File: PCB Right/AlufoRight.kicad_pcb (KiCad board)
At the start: 2 copper layers, 139.7 x 90.9 mm, 67 parts, among them J10 Shield_Connection, J2 USB_C_Receptacle_USB2.0_16P_2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, J4 USB_C_Receptacle_USB2.0_16P_2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, J6 Shield_Connection, J8 Shield_Connection, K11 PG1350, K12 PG1350, K13 PG1350, K14 PG1350, K15 PG1350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

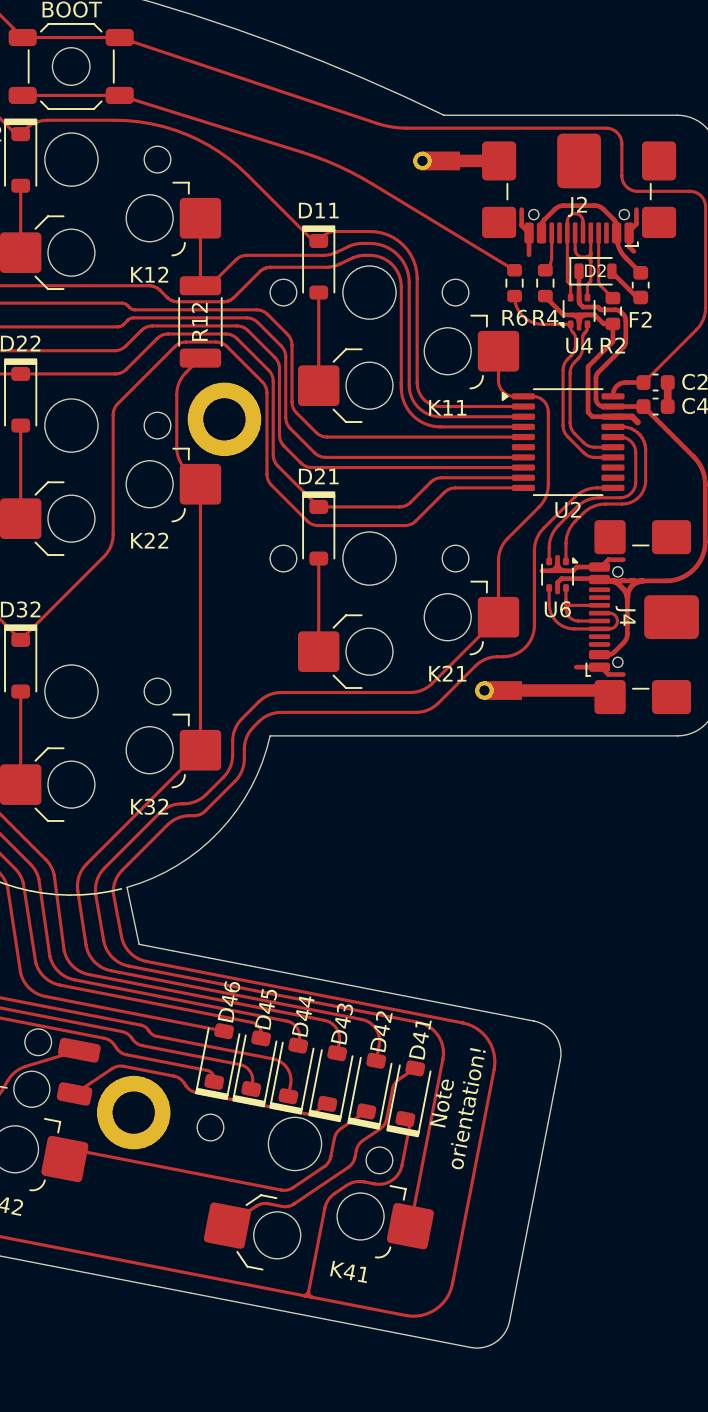
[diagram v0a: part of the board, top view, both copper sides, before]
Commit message: Tweak positioning of shield connections
Should now be the same on each side and align with other elements.
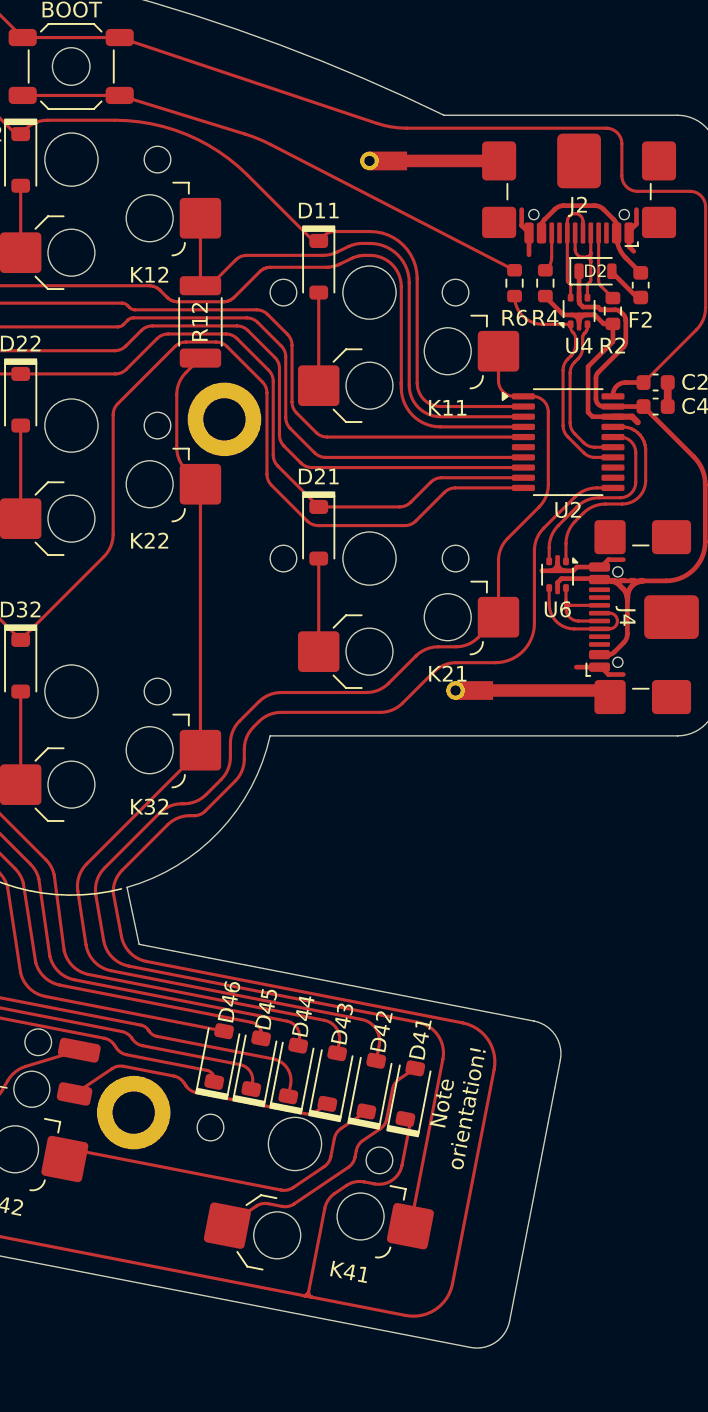
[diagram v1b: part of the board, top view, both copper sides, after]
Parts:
- moved J6 3.39 mm to (143.8, 44.0)
- moved J8 1.84 mm to (149.3, 77.9)
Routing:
- net Net-(J6-Pin_1): track 3.70 -> 7.09 mm
- net Net-(J8-Pin_1): track 6.41 -> 8.26 mm

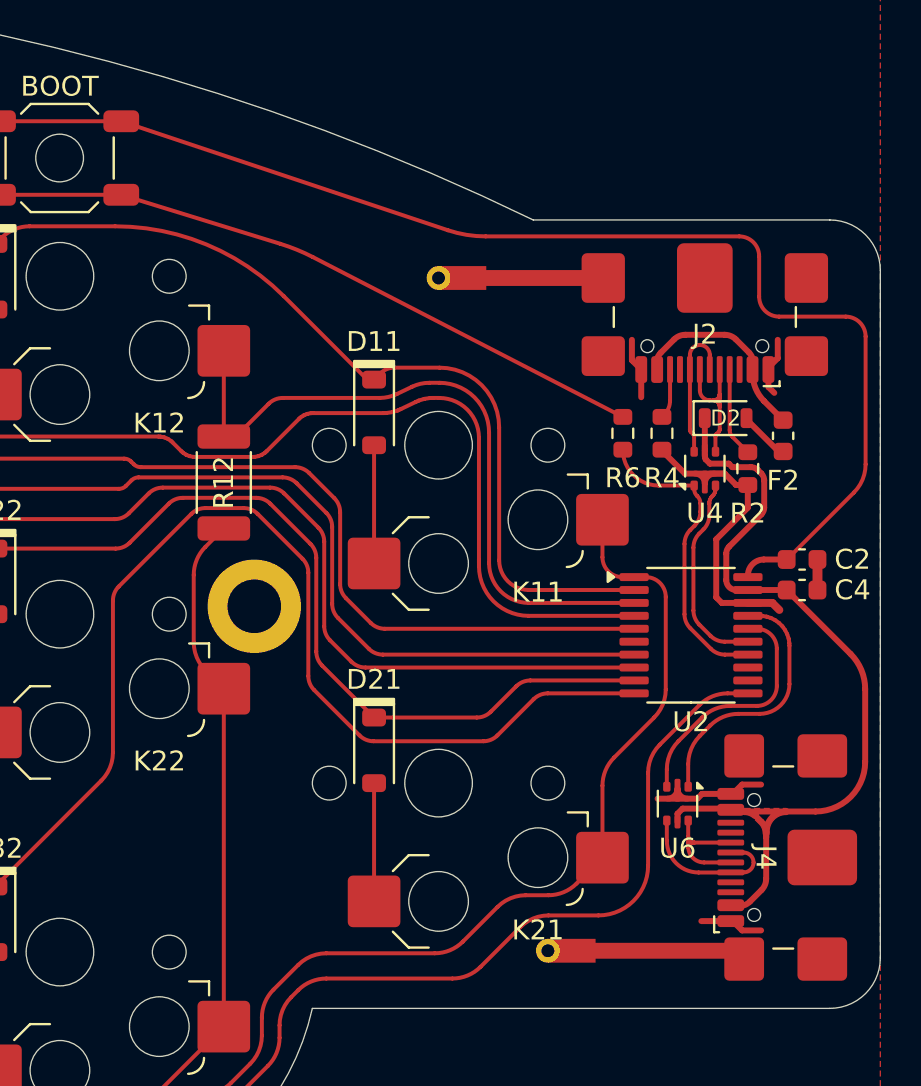
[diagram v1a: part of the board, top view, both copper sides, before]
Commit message: Minor tweaks
 * Relocate lefthand 5V decoupling capacitor
 * Alter spoke rotation on USB port A1 and A12 pads (this gives more ground connections when combined with B1 and B12)
 * Routing improvements
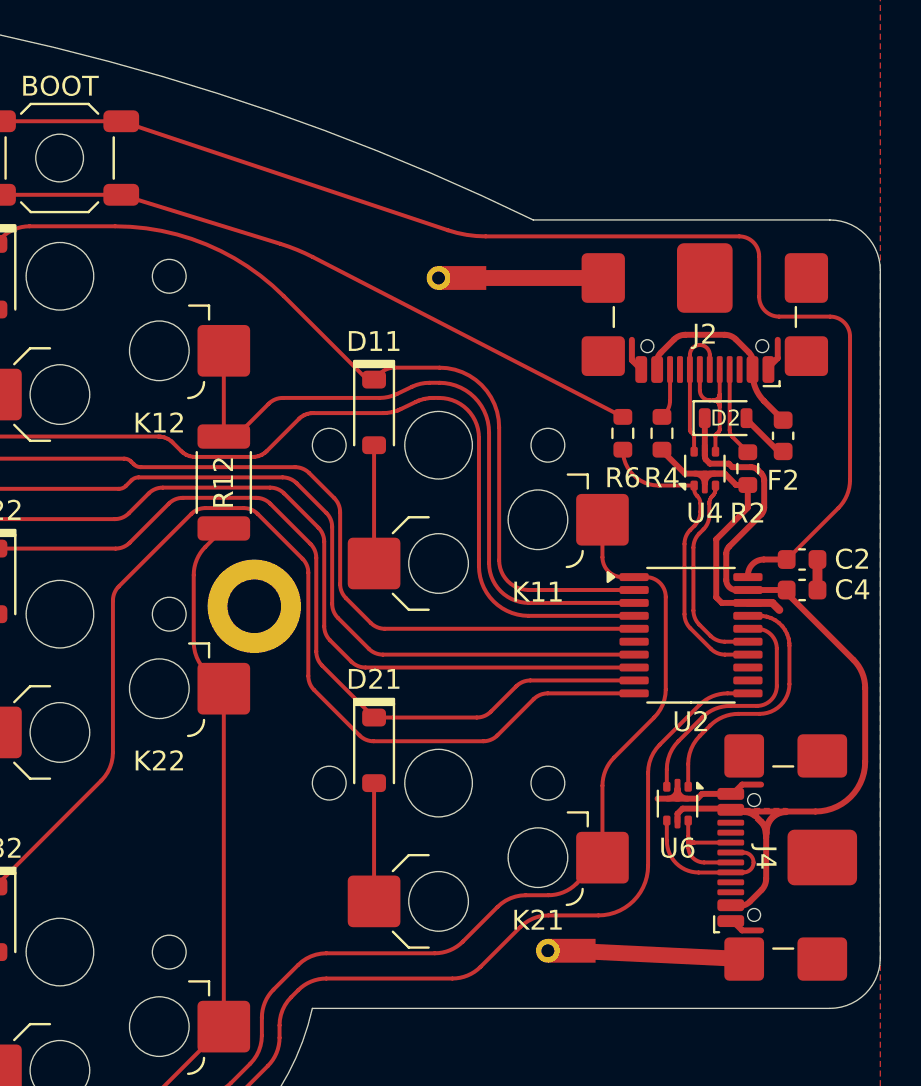
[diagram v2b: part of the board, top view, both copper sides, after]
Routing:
- net GND: track 27.8 -> 23.3 mm
- net +3V3: track 88.8 -> 87.7 mm
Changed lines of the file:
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@@
 			(pinfunction "GND")
 			(pintype "passive")
-			(thermal_bridge_angle 45)
 		)
 		(pad "A4" smd roundrect
@@
 			(pinfunction "GND")
 			(pintype "passive")
-			(thermal_bridge_angle 45)
 		)
 		(pad "B1" smd roundrect
@@
 		(descr "Hotswap footprint for Kailh Choc style switches")
 		(property "Reference" "K21"
-			(at 5 7.4 180)
+			(at 5 6.910317 180)
 			(layer "F.SilkS")
 			(effects
@@
 			(pinfunction "GND")
 			(pintype "passive")
-			(thermal_bridge_angle 45)
 		)
 		(pad "A4" smd roundrect
@@
 			(pinfunction "GND")
 			(pintype "passive")
-			(thermal_bridge_angle 45)
 		)
 		(pad "B1" smd roundrect
@@
 	)
 	(segment
-		(start 153.0705 48.508)
-		(end 153.0705 50.0025)
-		(width 0.3)
-		(layer "F.Cu")
-		(net 10)
-	)
-	(segment
-		(start 159.4705 49.4885)
-		(end 159.766 49.784)
-		(width 0.3)
-		(layer "F.Cu")
-		(net 10)
-	)
-	(segment
 		(start 152.6015 48.141)
 		(end 152.6015 47.114)
@@
 	)
 	(segment
-		(start 159.4705 48.508)
-		(end 159.4705 49.4885)
-		(width 0.3)
-		(layer "F.Cu")
-		(net 10)
-	)
-	(segment
 		(start 154.1145 52.688)
 		(end 155.2705 53.844)
@@
 	)
 	(segment
-		(start 157.675 76.358684)
-		(end 156.094684 76.358684)
-		(width 0.3)
-		(layer "F.Cu")
-		(net 10)
-	)
-	(segment
 		(start 159.9395 48.039)
 		(end 159.9395 47.114)
@@
 	)
 	(segment
+		(start 126.909593 36.116677)
+		(end 143.347506 41.601524)
+		(width 0.2)
+		(layer "F.Cu")
+		(net 19)
+	)
+	(segment
 		(start 116.966951 33.616676)
 		(end 96.2075 33.616676)
@@
 	)
 	(segment
-		(start 158.004 41.91)
-		(end 145.2466 41.91)
+		(start 162.990213 55.576787)
+		(end 160.401 58.166)
+		(width 0.2)
+		(layer "F.Cu")
+		(net 19)
+	)
+	(segment
+		(start 145.2466 41.91)
+		(end 158.004 41.91)
 		(width 0.2)
 		(layer "F.Cu")
@@
 	)
 	(segment
-		(start 143.347506 41.601524)
-		(end 126.909593 36.116677)
-		(width 0.2)
-		(layer "F.Cu")
-		(net 19)
-	)
-	(segment
-		(start 163.359 45.9456)
-		(end 160.004 45.9456)
+		(start 163.576 46.9456)
+		(end 163.576 54.162573)
 		(width 0.2)
 		(layer "F.Cu")
@@
 	)
 	(segment
-		(start 160.401 58.166)
-		(end 163.773214 54.793786)
-		(width 0.2)
-		(layer "F.Cu")
-		(net 19)
-	)
-	(segment
-		(start 164.359 53.379573)
-		(end 164.359 46.9456)
+		(start 159.004 42.91)
+		(end 159.004 44.9456)
 		(width 0.2)
 		(layer "F.Cu")
@@
 	)
 	(segment
-		(start 159.004 44.9456)
-		(end 159.004 42.91)
+		(start 160.004 45.9456)
+		(end 162.576 45.9456)
 		(width 0.2)
 		(layer "F.Cu")
@@
 	)
 	(arc
-		(start 160.004 45.9456)
-		(mid 159.296893 45.652707)
-		(end 159.004 44.9456)
+		(start 162.990213 55.576787)
+		(mid 163.423759 54.92794)
+		(end 163.576 54.162573)
 		(width 0.2)
 		(layer "F.Cu")
@@
 	)
 	(arc
-		(start 164.359 46.9456)
-		(mid 164.066107 46.238493)
-		(end 163.359 45.9456)
+		(start 159.004 44.9456)
+		(mid 159.296893 45.652707)
+		(end 160.004 45.9456)
 		(width 0.2)
 		(layer "F.Cu")
@@
 	)
 	(arc
-		(start 164.359 53.379573)
-		(mid 164.206759 54.14494)
-		(end 163.773214 54.793786)
+		(start 162.576 45.9456)
+		(mid 163.283107 46.238493)
+		(end 163.576 46.9456)
 		(width 0.2)
 		(layer "F.Cu")
@@
 	)
 	(arc
-		(start 145.2466 41.91)
+		(start 143.347506 41.601524)
 		(mid 144.284608 41.832379)
-		(end 143.347506 41.601524)
+		(end 145.2466 41.91)
 		(width 0.2)
 		(layer "F.Cu")
@@
 	)
 	(arc
-		(start 159.004 42.91)
-		(mid 158.711107 42.202893)
-		(end 158.004 41.91)
+		(start 119.088271 34.495355)
+		(mid 118.115001 33.845037)
+		(end 116.966951 33.616676)
 		(width 0.2)
 		(layer "F.Cu")
@@
 	)
 	(arc
-		(start 119.088271 34.495355)
-		(mid 118.115001 33.845037)
-		(end 116.966951 33.616676)
+		(start 158.004 41.91)
+		(mid 158.711107 42.202893)
+		(end 159.004 42.91)
 		(width 0.2)
 		(layer "F.Cu")
@@
 	)
 	(segment
-		(start 160.388 59.701)
-		(end 163.605767 62.918767)
-		(width 0.3)
-		(layer "F.Cu")
-		(net 21)
-	)
-	(segment
 		(start 157.65502 53.52)
 		(end 157.47802 53.343)
@@
 	)
 	(segment
-		(start 159.357 71.930055)
-		(end 159.357 71.875813)
+		(start 163.752213 63.219013)
+		(end 160.388 59.8548)
 		(width 0.3)
 		(layer "F.Cu")
@@
 	)
 	(segment
-		(start 157.349 59.201)
-		(end 157.349 57.869107)
+		(start 159.357 71.930055)
+		(end 159.357 71.875813)
 		(width 0.3)
 		(layer "F.Cu")
@@
 	)
 	(segment
-		(start 161.838 70.844684)
-		(end 160.357 70.844684)
+		(start 157.349 59.201)
+		(end 157.349 57.869107)
 		(width 0.3)
 		(layer "F.Cu")
@@
 	)
 	(segment
-		(start 164.338 64.686534)
-		(end 164.338 68.344684)
+		(start 156.311872 53.126737)
+		(end 156.272956 53.006972)
 		(width 0.3)
 		(layer "F.Cu")
@@
 	)
 	(segment
-		(start 156.311872 53.126737)
-		(end 156.272956 53.006972)
+		(start 160.357 70.844684)
+		(end 158.271629 70.844684)
 		(width 0.3)
 		(layer "F.Cu")
@@
 	)
 	(segment
-		(start 160.357 70.844684)
-		(end 158.271629 70.844684)
+		(start 164.338 68.344684)
+		(end 164.338 64.633227)
 		(width 0.3)
 		(layer "F.Cu")
@@
 	)
 	(segment
+		(start 160.357 70.844684)
+		(end 161.838 70.844684)
+		(width 0.3)
+		(layer "F.Cu")
+		(net 21)
+	)
+	(segment
 		(start 159.357 72.136)
 		(end 159.357 74.230313)
@@
 	)
 	(arc
+		(start 161.838 70.844684)
+		(mid 163.605767 70.112451)
+		(end 164.338 68.344684)
+		(width 0.3)
+		(layer "F.Cu")
+		(net 21)
+	)
+	(arc
 		(start 159.111054 55.899946)
 		(mid 159.21944 55.737734)
@@
 	)
 	(arc
-		(start 164.338 68.344684)
-		(mid 163.605767 70.112451)
-		(end 161.838 70.844684)
-		(width 0.3)
-		(layer "F.Cu")
-		(net 21)
-	)
-	(arc
 		(start 158.544314 75.37437)
 		(mid 158.284775 75.547788)
@@
 	)
 	(arc
-		(start 163.605767 62.918767)
-		(mid 164.147699 63.729825)
-		(end 164.338 64.686534)
+		(start 158.93972 53.666446)
+		(mid 158.777508 53.55806)
+		(end 158.586167 53.52)
 		(width 0.3)
 		(layer "F.Cu")
@@
 	)
 	(arc
-		(start 158.93972 53.666446)
-		(mid 158.777508 53.55806)
-		(end 158.586167 53.52)
+		(start 163.752213 63.219013)
+		(mid 164.185759 63.86786)
+		(end 164.338 64.633227)
 		(width 0.3)
 		(layer "F.Cu")
@@
 	)
 	(segment
-		(start 157.832316 77.851)
+		(start 158.25 78.268684)
 		(end 149.575 77.851)
 		(width 0.8)
